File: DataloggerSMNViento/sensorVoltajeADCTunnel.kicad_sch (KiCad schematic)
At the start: 7 parts

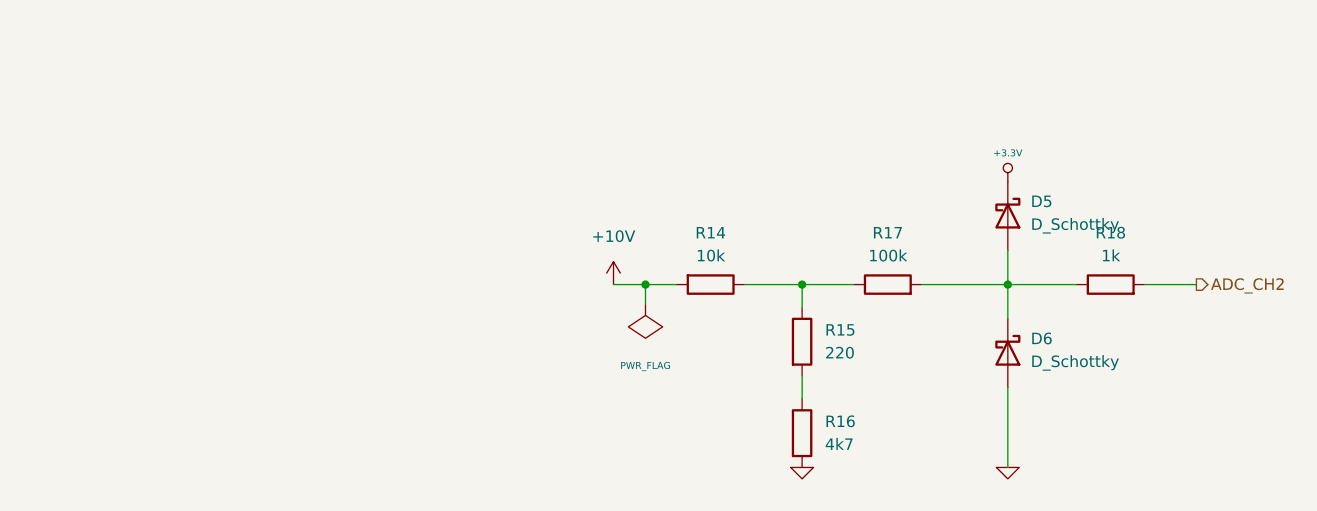
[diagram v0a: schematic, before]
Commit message: Subo la version v1.0 del PCB del poncho de la tesis
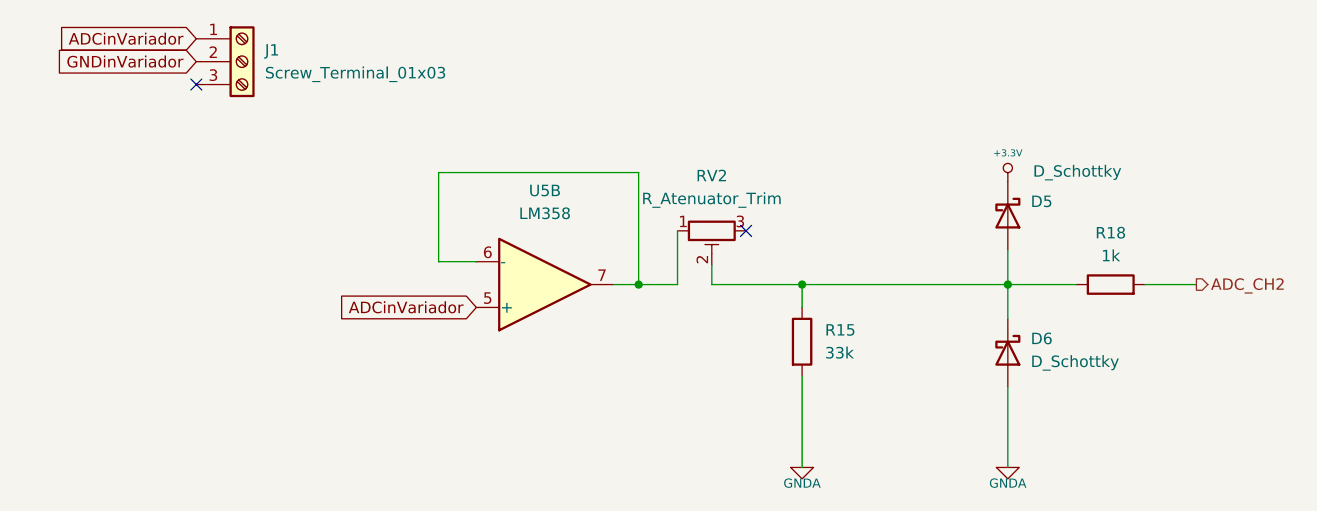
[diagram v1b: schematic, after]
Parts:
- removed R14: 10k, Resistor_THT:R_Axial_DIN0207_L6.3mm_D2.5mm_P15.24mm_Horizontal, symbol Device:R
- removed R16: 4k7, Resistor_THT:R_Axial_DIN0207_L6.3mm_D2.5mm_P15.24mm_Horizontal, symbol Device:R
- removed R17: 100k, Resistor_THT:R_Axial_DIN0207_L6.3mm_D2.5mm_P15.24mm_Horizontal, symbol Device:R
- added J1: Screw_Terminal_01x03, TerminalBlock:TerminalBlock_Altech_AK300-3_P5.00mm, symbol Connector:Screw_Terminal_01x03
- added RV2: R_Atenuator_Trim, Connector_PinHeader_2.54mm:PinHeader_1x03_P2.54mm_Vertical, symbol Device:R_Potentiometer_Trim
- added U5: LM358, Package_SO:SO-8_3.9x4.9mm_P1.27mm, symbol Amplifier_Operational:LM358
- D5, D6: footprint Diode_THT:D_DO-41_SOD81_P10.16mm_Horizontal -> Diode_SMD:D_2010_5025Metric
- R15: value 220 -> 33k; footprint Resistor_THT:R_Axial_DIN0207_L6.3mm_D2.5mm_P15.24mm_Horizontal -> Resistor_SMD:R_1206_3216Metric
- R18: footprint Resistor_THT:R_Axial_DIN0207_L6.3mm_D2.5mm_P15.24mm_Horizontal -> Resistor_SMD:R_1206_3216Metric
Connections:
- net GND is gone; now on net GNDA: D6.2 (A)
- net at R15.1: now also D5.2 (A), D6.1 (K), R18.1, RV2.2
- net GNDA: now reaches R15.2
- new net: RV2.1, U5.6 (-), U5.7
- new net ADCinVariador: J1.1 (Pin_1), U5.5 (+)
- new net GNDinVariador: J1.2 (Pin_2)
- no-connect marks 0 -> 2

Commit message: Se debe cambiar el diseño porque el footprint del  StepDown esta invertido, lo cual va a implicar cambiar algunas pistas
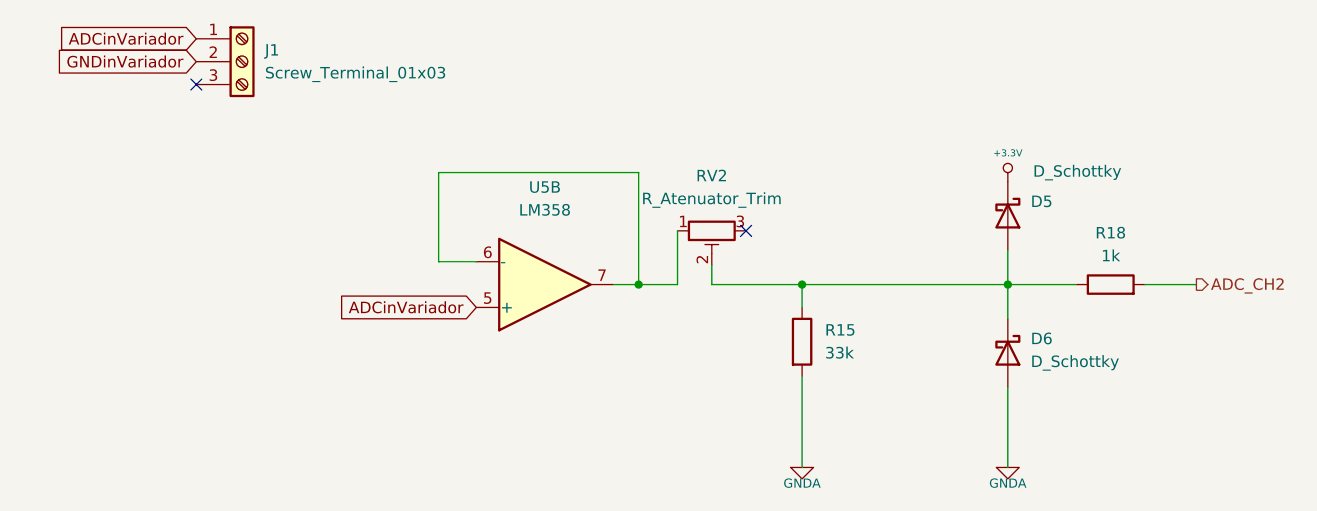
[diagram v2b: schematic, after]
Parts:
- D5, D6: footprint Diode_SMD:D_2010_5025Metric -> Diode_SMD:D_SOD-128
- U5: footprint Package_SO:SO-8_3.9x4.9mm_P1.27mm -> Package_SO:SOIC-8_3.9x4.9mm_P1.27mm
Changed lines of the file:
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@@
   (symbol (lib_id "Amplifier_Operational:LM358") (at 94.615 59.055 0) (mirror x) (unit 2)
     (in_bom yes) (on_board yes) (fields_autoplaced)
-    (property "Reference" "U5" (id 0) (at 94.615 48.641 0))
-    (property "Value" "LM358" (id 1) (at 94.615 51.181 0))
-    (property "Footprint" "Package_SO:SO-8_3.9x4.9mm_P1.27mm" (id 2) (at 94.615 59.055 0)
+    (property "Reference" "U5" (id 0) (at 94.615 48.26 0))
+    (property "Value" "LM358" (id 1) (at 94.615 50.8 0))
+    (property "Footprint" "Package_SO:SOIC-8_3.9x4.9mm_P1.27mm" (id 2) (at 94.615 59.055 0)
       (effects (font (size 1.27 1.27)) hide)
     )
@@
       (effects (font (size 1.27 1.27)) (justify left))
     )
-    (property "Footprint" "Diode_SMD:D_2010_5025Metric" (id 2) (at 146.05 66.675 0)
+    (property "Footprint" "Diode_SMD:D_SOD-128" (id 2) (at 146.05 66.675 0)
       (effects (font (size 1.27 1.27)) hide)
     )
@@
       (effects (font (size 1.27 1.27)) (justify left))
     )
-    (property "Footprint" "Diode_SMD:D_2010_5025Metric" (id 2) (at 146.05 51.435 0)
+    (property "Footprint" "Diode_SMD:D_SOD-128" (id 2) (at 146.05 51.435 0)
       (effects (font (size 1.27 1.27)) hide)
     )
